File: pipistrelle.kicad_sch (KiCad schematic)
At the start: 67 parts, among them J1 C2M, J2 C2F, J3 Eurorack Power, J4 CV1, J5 V/OCT, J6 OUT, J7 CV2, J8 C1M, J9 C1F, U1 SeeeduinoXIAO, U2 MCP6002-xSN, U3 MCP6002-xSN, U4 TL072, U5 LM1117-5.0, U6 LM4040DBZ-10

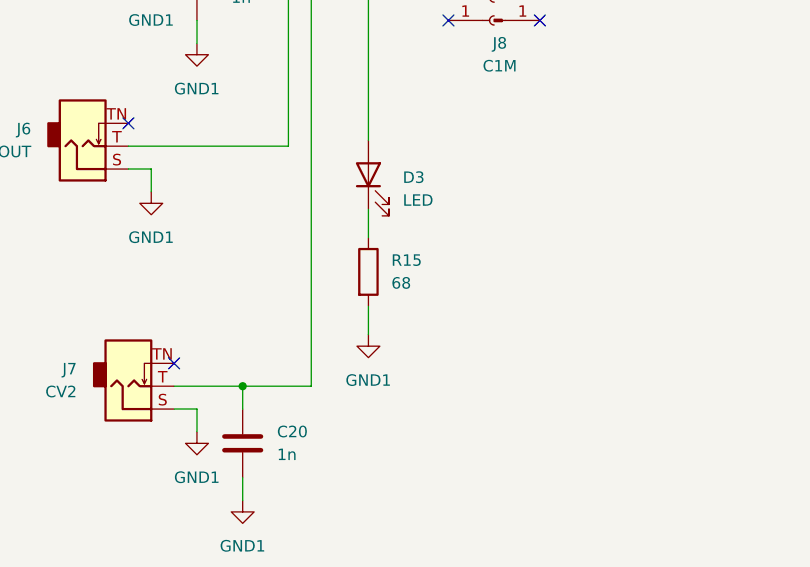
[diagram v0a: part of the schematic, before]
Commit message: Use 1k for LED resistor
Tested, and plenty bright enough.
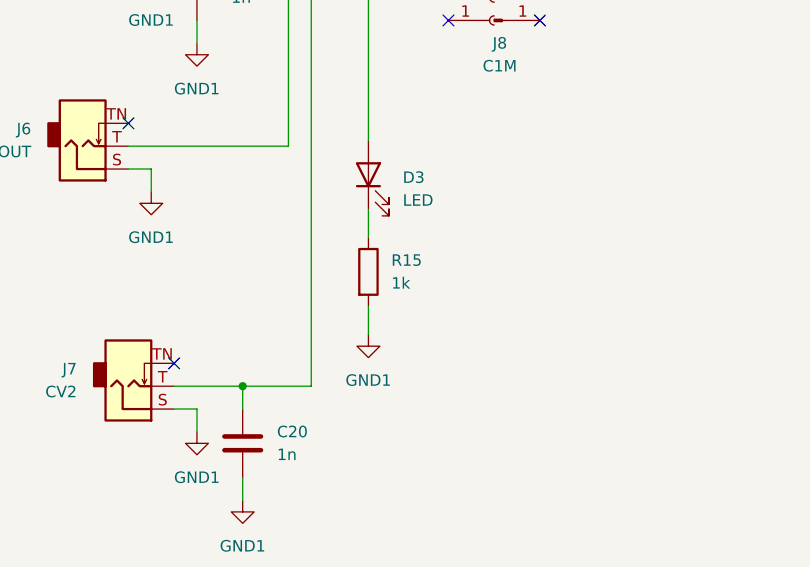
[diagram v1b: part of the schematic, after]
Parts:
- R15: value 68 -> 1k
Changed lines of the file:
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@@
       (effects (font (size 1.27 1.27)) (justify left))
     )
-    (property "Value" "68" (id 1) (at 350.52 175.2599 0)
+    (property "Value" "1k" (id 1) (at 350.52 175.2599 0)
       (effects (font (size 1.27 1.27)) (justify left))
     )
@@
     )
     (path "/b774936c-04f2-44d8-ad21-e9c8c3f13f9b"
-      (reference "R15") (unit 1) (value "68") (footprint "Resistor_SMD:R_0603_1608Metric")
+      (reference "R15") (unit 1) (value "1k") (footprint "Resistor_SMD:R_0603_1608Metric")
     )
     (path "/6869eb04-eef5-4314-b662-7073f10a443e"

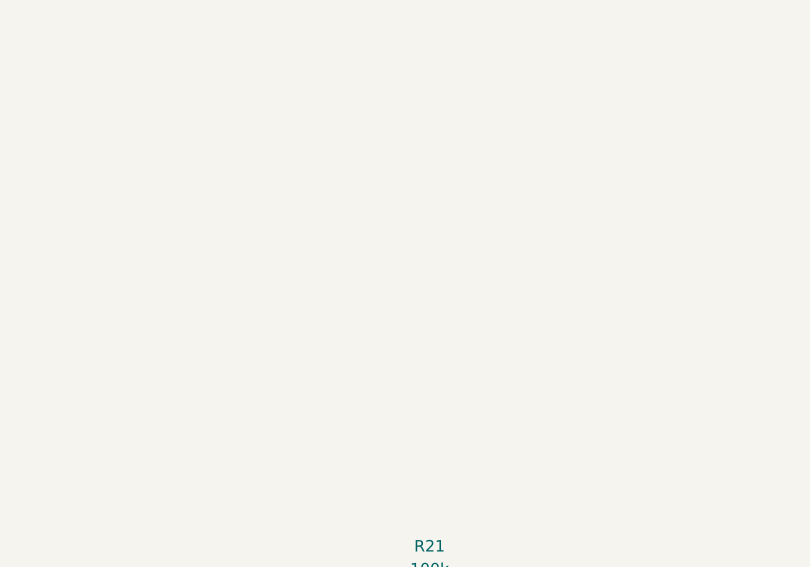
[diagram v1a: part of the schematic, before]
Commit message: Update footprints
Mouse bites are now in the schematic so they won't disappear on update
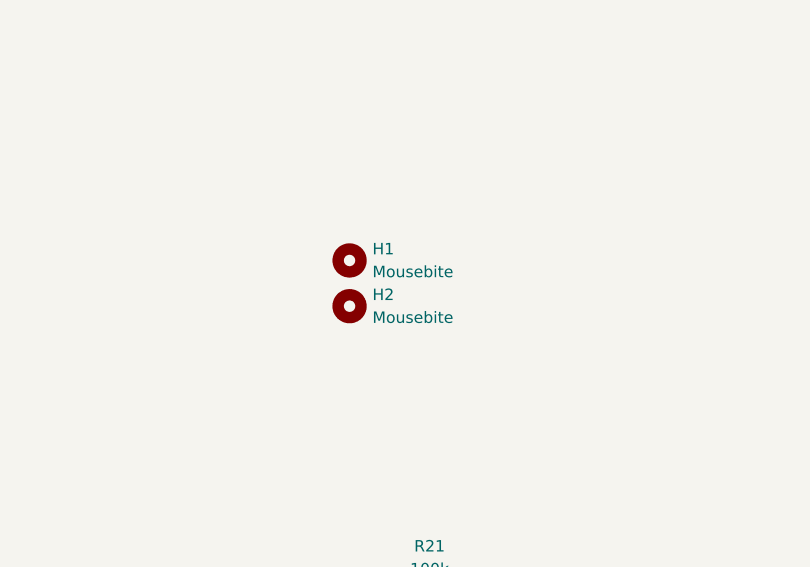
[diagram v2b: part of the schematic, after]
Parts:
- added H1, H2: Mousebite, Personal:Mouse_bite_2x5mm, symbol Mechanical:MountingHole
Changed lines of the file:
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@@
     (pin "6")
+  )
+  (symbol (lib_id "Mechanical:MountingHole") (at 215.9 114.3 0) (unit 1)
+    (in_bom yes) (on_board yes) (fields_autoplaced)
+    (property "Reference" "H2" (id 0) (at 218.44 113.0299 0)
+      (effects (font (size 1.27 1.27)) (justify left))
+    )
+    (property "Value" "Mousebite" (id 1) (at 218.44 115.5699 0)
+      (effects (font (size 1.27 1.27)) (justify left))
+    )
+    (property "Footprint" "Personal:Mouse_bite_2x5mm" (id 2) (at 215.9 114.3 0)
+      (effects (font (size 1.27 1.27)) hide)
+    )
+    (property "Datasheet" "~" (id 3) (at 215.9 114.3 0)
+      (effects (font (size 1.27 1.27)) hide)
+    )
   )
   (symbol (lib_id "Connector:AudioJack2_SwitchT") (at 316.23 160.02 0) (mirror x) (unit 1)
@@
     )
     (pin "1")
+  )
+  (symbol (lib_id "Mechanical:MountingHole") (at 215.9 109.22 0) (unit 1)
+    (in_bom yes) (on_board yes) (fields_autoplaced)
+    (property "Reference" "H1" (id 0) (at 218.44 107.9499 0)
+      (effects (font (size 1.27 1.27)) (justify left))
+    )
+    (property "Value" "Mousebite" (id 1) (at 218.44 110.4899 0)
+      (effects (font (size 1.27 1.27)) (justify left))
+    )
+    (property "Footprint" "Personal:Mouse_bite_2x5mm" (id 2) (at 215.9 109.22 0)
+      (effects (font (size 1.27 1.27)) hide)
+    )
+    (property "Datasheet" "~" (id 3) (at 215.9 109.22 0)
+      (effects (font (size 1.27 1.27)) hide)
+    )
   )
   (symbol (lib_id "Amplifier_Operational:TL072") (at 173.99 165.1 0) (mirror x) (unit 2)
@@
       (reference "D3") (unit 1) (value "LED") (footprint "LED_THT:LED_D3.0mm")
     )
+    (path "/9c97db98-dfe2-455c-80b1-cf93c801bc35"
+      (reference "H1") (unit 1) (value "Mousebite") (footprint "Personal:Mouse_bite_2x5mm")
+    )
+    (path "/882ea305-cc45-466a-9378-45336f1576b5"
+      (reference "H2") (unit 1) (value "Mousebite") (footprint "Personal:Mouse_bite_2x5mm")
+    )
     (path "/6ce08c78-8e2a-4b96-af2b-67e3b815dc24"

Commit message: Change ESD cap to 1206
The 0603 I intended to use is unavailable at JLC, and there's plenty of
space.
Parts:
- C18, C19, C20: footprint Capacitor_SMD:C_0603_1608Metric -> Capacitor_SMD:C_1206_3216Metric
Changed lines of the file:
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@@
       (effects (font (size 1.27 1.27)) (justify left))
     )
-    (property "Footprint" "Capacitor_SMD:C_0603_1608Metric" (id 2) (at 334.9752 123.19 0)
+    (property "Footprint" "Capacitor_SMD:C_1206_3216Metric" (id 2) (at 334.9752 123.19 0)
       (effects (font (size 1.27 1.27)) hide)
     )
@@
       (effects (font (size 1.27 1.27)) (justify left))
     )
-    (property "Footprint" "Capacitor_SMD:C_0603_1608Metric" (id 2) (at 334.9752 196.85 0)
+    (property "Footprint" "Capacitor_SMD:C_1206_3216Metric" (id 2) (at 334.9752 196.85 0)
       (effects (font (size 1.27 1.27)) hide)
     )
@@
       (effects (font (size 1.27 1.27)) (justify left))
     )
-    (property "Footprint" "Capacitor_SMD:C_0603_1608Metric" (id 2) (at 329.8952 146.05 0)
+    (property "Footprint" "Capacitor_SMD:C_1206_3216Metric" (id 2) (at 329.8952 146.05 0)
       (effects (font (size 1.27 1.27)) hide)
     )
@@
     )
     (path "/f118a79a-955e-4c66-b529-7fecd96a0b6d"
-      (reference "C18") (unit 1) (value "1n") (footprint "Capacitor_SMD:C_0603_1608Metric")
+      (reference "C18") (unit 1) (value "1n") (footprint "Capacitor_SMD:C_1206_3216Metric")
     )
     (path "/5fb53d5c-4291-47a6-9ad1-0578fcc65cf7"
-      (reference "C19") (unit 1) (value "1n") (footprint "Capacitor_SMD:C_0603_1608Metric")
+      (reference "C19") (unit 1) (value "1n") (footprint "Capacitor_SMD:C_1206_3216Metric")
     )
     (path "/8c0bcb78-d6b0-44a1-8522-f4df214a0c4f"
-      (reference "C20") (unit 1) (value "1n") (footprint "Capacitor_SMD:C_0603_1608Metric")
+      (reference "C20") (unit 1) (value "1n") (footprint "Capacitor_SMD:C_1206_3216Metric")
     )
     (path "/5c9f8e74-305b-4db3-a04e-3ef2f1373b22"

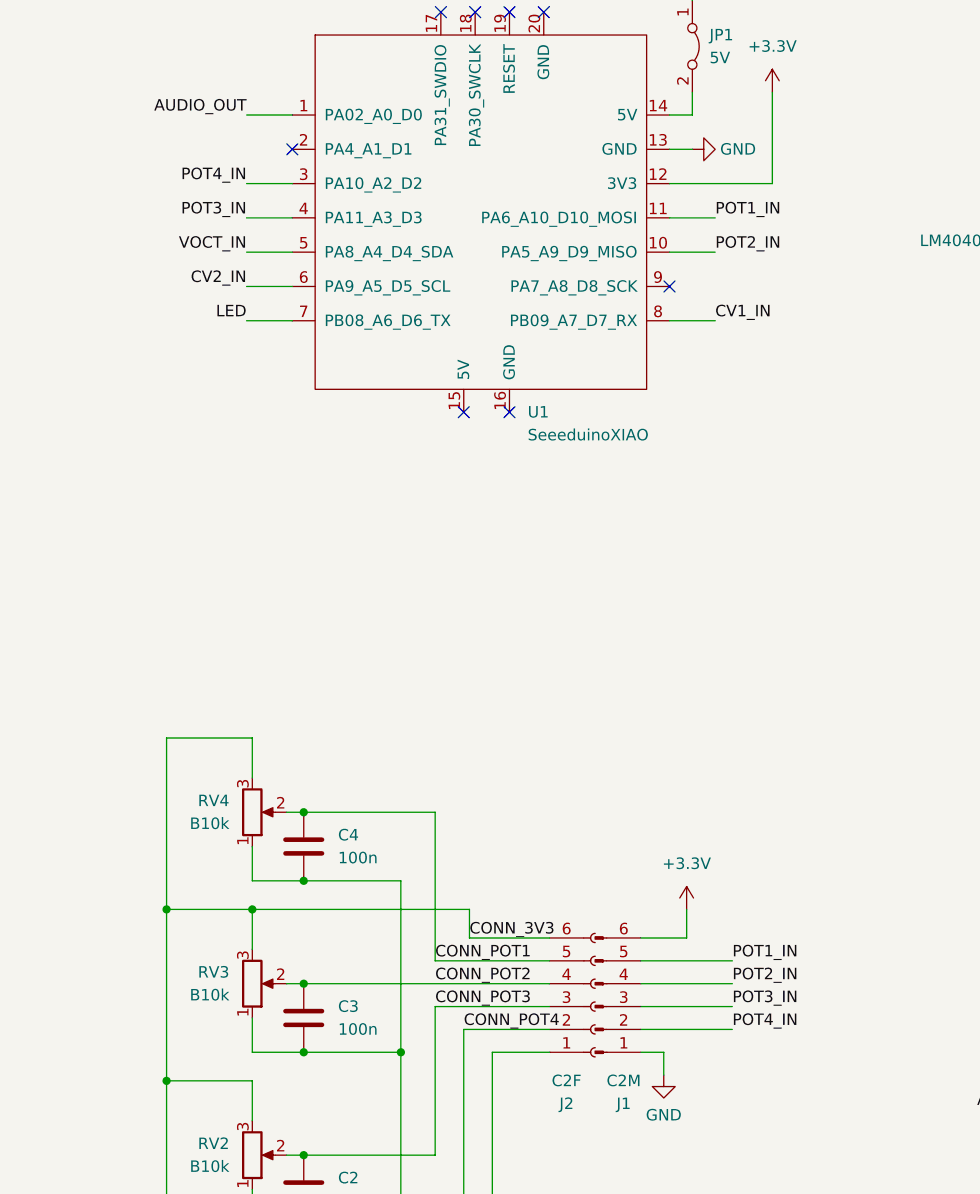
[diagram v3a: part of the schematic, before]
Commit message: Use ABCD for pot designations as front panel
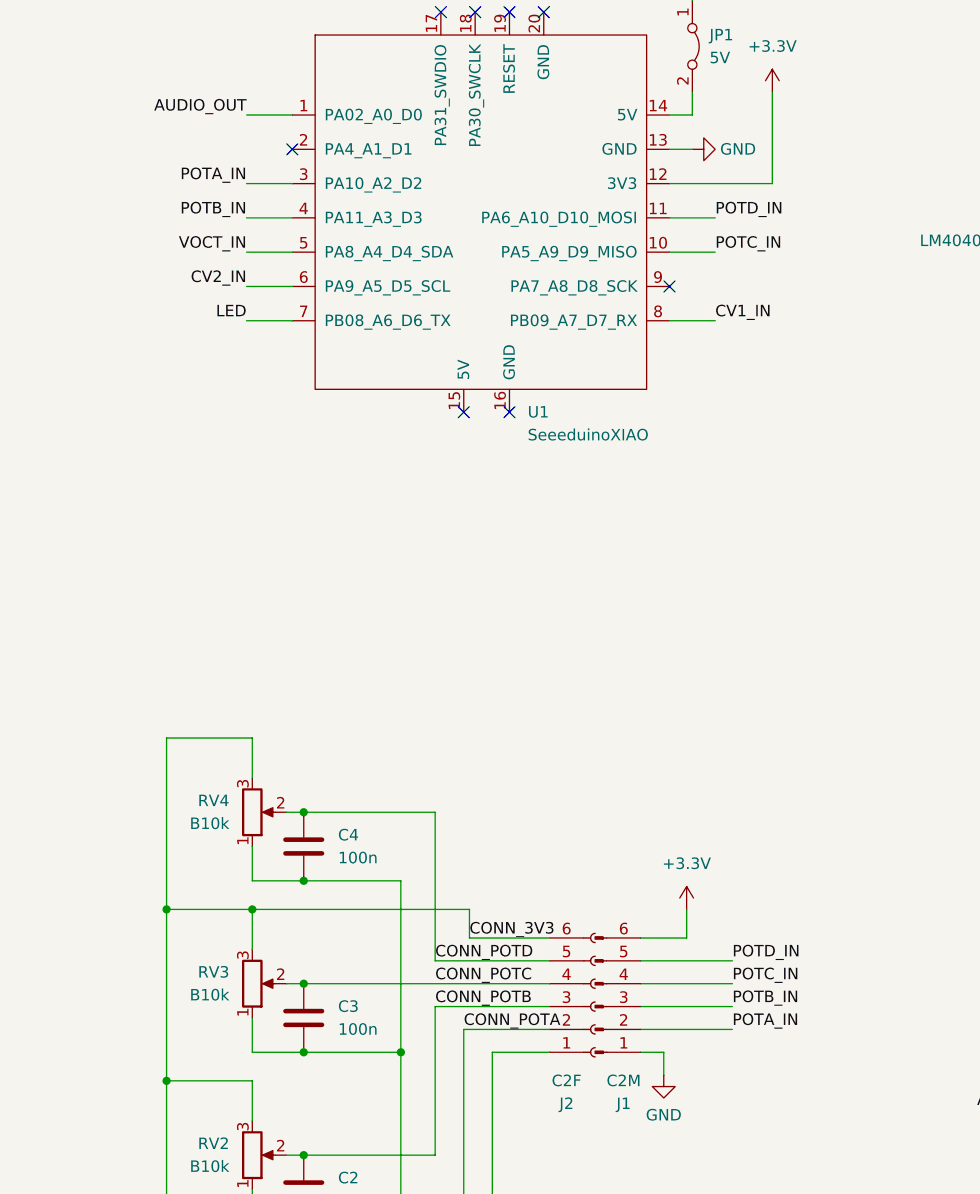
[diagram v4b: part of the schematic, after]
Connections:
- net CONN_POT1 renamed CONN_POTD
- net CONN_POT2 renamed CONN_POTC
- net CONN_POT3 renamed CONN_POTB
- net CONN_POT4 renamed CONN_POTA
- net POT1_IN renamed POTD_IN
- net POT2_IN renamed POTC_IN
- net POT3_IN renamed POTB_IN
- net POT4_IN renamed POTA_IN
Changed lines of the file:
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@@
     (effects (font (size 1.27 1.27)) (justify right bottom))
   )
-  (label "CONN_POT3" (at 78.105 151.13 0)
+  (label "CONN_POTB" (at 78.105 151.13 0)
     (effects (font (size 1.27 1.27)) (justify left bottom))
   )
-  (label "POT2_IN" (at 111.125 148.59 0)
+  (label "POTC_IN" (at 111.125 148.59 0)
     (effects (font (size 1.27 1.27)) (justify left bottom))
   )
@@
     (effects (font (size 1.27 1.27)) (justify left bottom))
   )
-  (label "CONN_POT1" (at 78.105 146.05 0)
+  (label "CONN_POTD" (at 78.105 146.05 0)
     (effects (font (size 1.27 1.27)) (justify left bottom))
   )
@@
     (effects (font (size 1.27 1.27)) (justify left bottom))
   )
-  (label "POT2_IN" (at 109.22 67.31 0)
+  (label "POTC_IN" (at 109.22 67.31 0)
     (effects (font (size 1.27 1.27)) (justify left bottom))
   )
-  (label "POT3_IN" (at 111.125 151.13 0)
+  (label "POTB_IN" (at 111.125 151.13 0)
     (effects (font (size 1.27 1.27)) (justify left bottom))
   )
@@
     (effects (font (size 1.27 1.27)) (justify left bottom))
   )
-  (label "POT4_IN" (at 57.15 59.69 180)
+  (label "POTA_IN" (at 57.15 59.69 180)
     (effects (font (size 1.27 1.27)) (justify right bottom))
   )
@@
     (effects (font (size 1.27 1.27)) (justify left bottom))
   )
-  (label "POT1_IN" (at 111.125 146.05 0)
+  (label "POTD_IN" (at 111.125 146.05 0)
     (effects (font (size 1.27 1.27)) (justify left bottom))
   )
-  (label "CONN_POT4" (at 81.28 153.67 0)
+  (label "CONN_POTA" (at 81.28 153.67 0)
     (effects (font (size 1.27 1.27)) (justify left bottom))
   )
-  (label "POT1_IN" (at 109.22 63.5 0)
+  (label "POTD_IN" (at 109.22 63.5 0)
     (effects (font (size 1.27 1.27)) (justify left bottom))
   )
@@
     (effects (font (size 1.27 1.27)) (justify right bottom))
   )
-  (label "POT3_IN" (at 57.15 63.5 180)
+  (label "POTB_IN" (at 57.15 63.5 180)
     (effects (font (size 1.27 1.27)) (justify right bottom))
   )
@@
     (effects (font (size 1.27 1.27)) (justify right bottom))
   )
-  (label "POT4_IN" (at 111.125 153.67 0)
+  (label "POTA_IN" (at 111.125 153.67 0)
     (effects (font (size 1.27 1.27)) (justify left bottom))
   )
@@
     (effects (font (size 1.27 1.27)) (justify left bottom))
   )
-  (label "CONN_POT2" (at 78.105 148.59 0)
+  (label "CONN_POTC" (at 78.105 148.59 0)
     (effects (font (size 1.27 1.27)) (justify left bottom))
   )

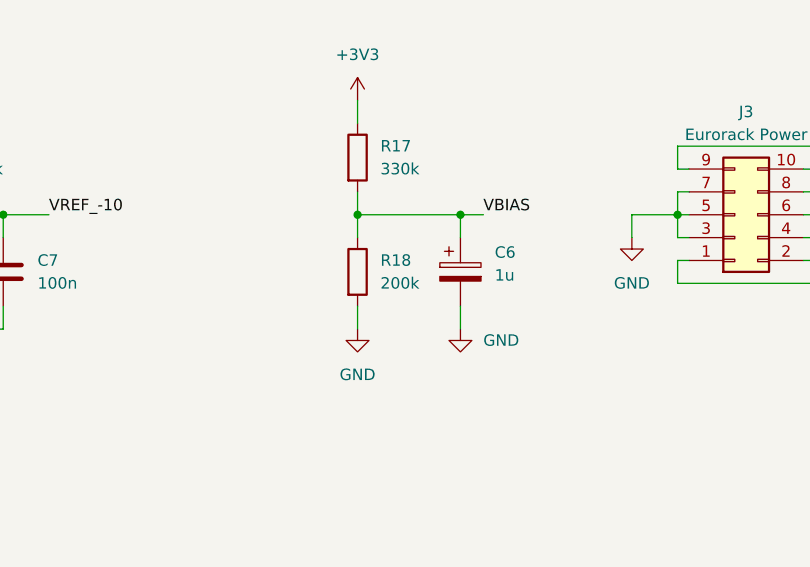
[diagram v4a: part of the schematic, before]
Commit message: Correct output offset
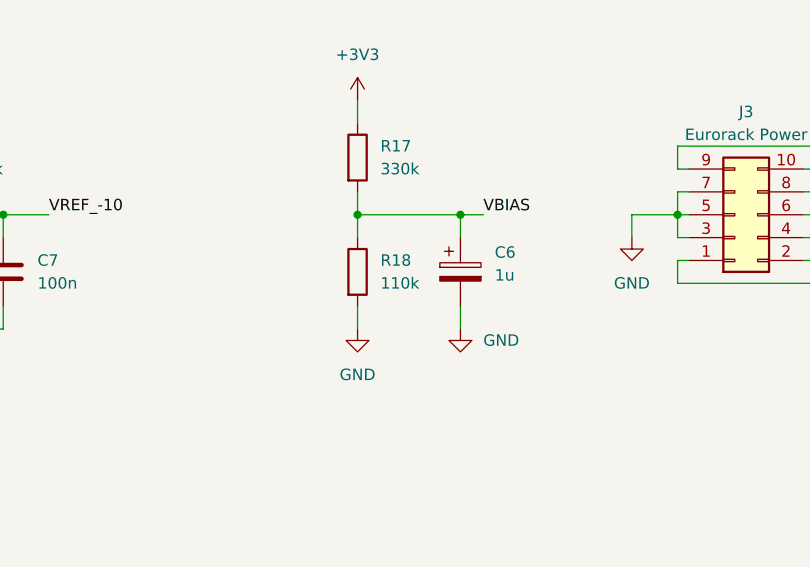
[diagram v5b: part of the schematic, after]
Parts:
- R18: value 200k -> 110k
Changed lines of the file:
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@@
       (effects (font (size 1.27 1.27)) (justify left))
     )
-    (property "Value" "200k" (id 1) (at 196.85 66.0399 0)
+    (property "Value" "110k" (id 1) (at 196.85 66.0399 0)
       (effects (font (size 1.27 1.27)) (justify left))
     )
@@
     )
     (path "/4131b36a-87fa-4a01-8dd9-32e1175455b4"
-      (reference "R18") (unit 1) (value "200k") (footprint "Resistor_SMD:R_0603_1608Metric")
+      (reference "R18") (unit 1) (value "110k") (footprint "Resistor_SMD:R_0603_1608Metric")
     )
     (path "/7b2d4d72-2c2c-4e83-b34a-cc6d4eeffbfd"

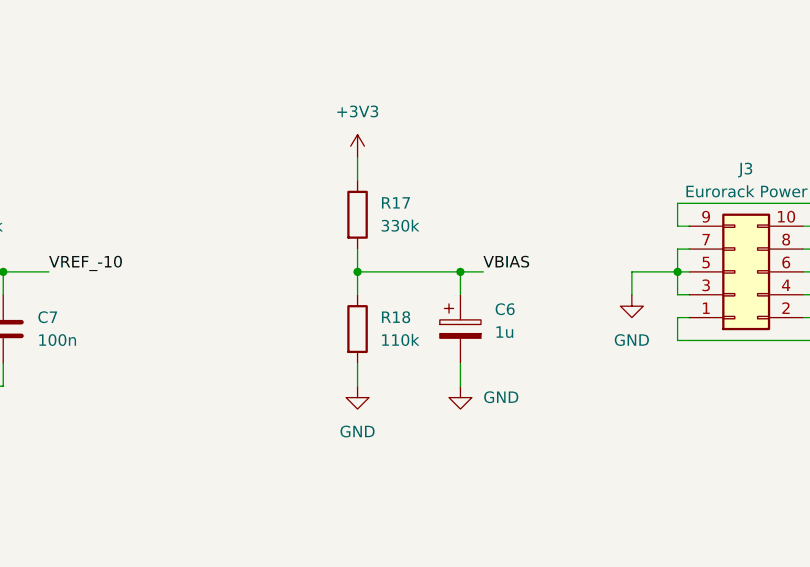
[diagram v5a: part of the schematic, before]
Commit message: Use more common values for offset divider
Neither 110 nor 300 are E12, but 100 is E6.
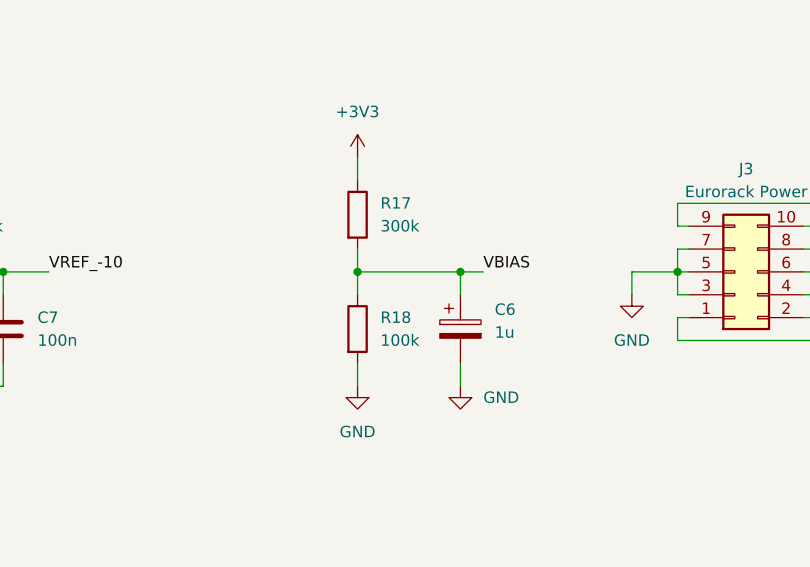
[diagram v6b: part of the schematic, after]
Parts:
- R17: value 330k -> 300k
- R18: value 110k -> 100k
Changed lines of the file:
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@@
       (effects (font (size 1.27 1.27)) (justify left))
     )
-    (property "Value" "330k" (id 1) (at 196.85 53.3399 0)
+    (property "Value" "300k" (id 1) (at 196.85 53.3399 0)
       (effects (font (size 1.27 1.27)) (justify left))
     )
@@
       (effects (font (size 1.27 1.27)) (justify left))
     )
-    (property "Value" "110k" (id 1) (at 196.85 66.0399 0)
+    (property "Value" "100k" (id 1) (at 196.85 66.0399 0)
       (effects (font (size 1.27 1.27)) (justify left))
     )
@@
     )
     (path "/29fc90ae-e4d8-4149-8efb-10c6c84a0eb3"
-      (reference "R17") (unit 1) (value "330k") (footprint "Resistor_SMD:R_0603_1608Metric")
+      (reference "R17") (unit 1) (value "300k") (footprint "Resistor_SMD:R_0603_1608Metric")
     )
     (path "/4131b36a-87fa-4a01-8dd9-32e1175455b4"
-      (reference "R18") (unit 1) (value "110k") (footprint "Resistor_SMD:R_0603_1608Metric")
+      (reference "R18") (unit 1) (value "100k") (footprint "Resistor_SMD:R_0603_1608Metric")
     )
     (path "/7b2d4d72-2c2c-4e83-b34a-cc6d4eeffbfd"
